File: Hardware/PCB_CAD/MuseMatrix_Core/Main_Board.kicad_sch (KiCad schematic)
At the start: 16 parts, among them J10 Conn_01x03_Pin, J11 Conn_01x03_Pin, J12 Conn_01x03_Pin, J14 Jack-DC, J4 DIN-5, J5 Conn_01x07_Socket, J6 Conn_01x03_Pin, J7 Conn_01x03_Pin, J8 Conn_01x03_Pin, J9 Conn_01x03_Pin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

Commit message: update
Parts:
- J5: value Conn_01x07_Socket -> Conn_01x10_Socket; footprint Connector_JST:JST_EH_B7B-EH-A_1x07_P2.50mm_Vertical -> Library:Skedd connector x10
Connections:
- net jst0: now also J5.1 (Pin_1)
- no-connect marks 4 -> 7
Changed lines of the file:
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@@
 	(paper "A4")
+	(junction
+		(at 38.1 58.38)
+		(diameter 0)
+		(color 0 0 0 0)
+	)
+	(junction
+		(at 38.1 66)
+		(diameter 0)
+		(color 0 0 0 0)
+	)
+	(junction
+		(at 38.1 63.46)
+		(diameter 0)
+		(color 0 0 0 0)
+	)
 	(junction
 		(at 218.6 132.4626)
@@
 	)
 	(junction
+		(at 38.26 68.54)
+		(diameter 0)
+		(color 0 0 0 0)
+	)
+	(junction
 		(at 202 156.3)
+		(diameter 0)
+		(color 0 0 0 0)
+	)
+	(junction
+		(at 38.1 55.88)
+		(diameter 0)
+		(color 0 0 0 0)
+	)
+	(junction
+		(at 37.6 53.34)
 		(diameter 0)
 		(color 0 0 0 0)
@@
 		(color 0 0 0 0)
 	)
+	(junction
+		(at 38.1 60.92)
+		(diameter 0)
+		(color 0 0 0 0)
+	)
+	(no_connect
+		(at 39 71.08)
+	)
 	(no_connect
 		(at 201.08 139.66)
 	)
 	(no_connect
+		(at 39 73.62)
+	)
+	(no_connect
+		(at 39 76.16)
+	)
+	(no_connect
 		(at 208.7 134.58)
 	)
@@
 	(wire
 		(pts
-			(xy 38 63.46) (xy 39 63.46)
+			(xy 36.83 68.58) (xy 36.83 68.54)
+		)
+		(stroke
+			(width 0)
+			(type default)
+		)
+	)
+	(wire
+		(pts
+			(xy 38 63.46) (xy 38.1 63.46)
 		)
 		(stroke
@@
 	(wire
 		(pts
+			(xy 37.6 53.34) (xy 39 53.34)
+		)
+		(stroke
+			(width 0)
+			(type default)
+		)
+	)
+	(wire
+		(pts
+			(xy 38.1 55.88) (xy 39 55.84)
+		)
+		(stroke
+			(width 0)
+			(type default)
+		)
+	)
+	(wire
+		(pts
 			(xy 178.189 131.04) (xy 178.189 131.0479)
 		)
@@
 	(wire
 		(pts
-			(xy 37.8 58.38) (xy 39 58.38)
+			(xy 38.1 66.04) (xy 38.1 66)
+		)
+		(stroke
+			(width 0)
+			(type default)
+		)
+	)
+	(wire
+		(pts
+			(xy 37.8 58.38) (xy 38.1 58.38)
 		)
 		(stroke
@@
 	(wire
 		(pts
-			(xy 38.1 53.4) (xy 39 53.4)
-		)
-		(stroke
-			(width 0)
-			(type default)
-		)
-	)
-	(wire
-		(pts
 			(xy 194.3 128.5) (xy 195.8 128.5)
 		)
@@
 	(wire
 		(pts
-			(xy 37.6 53.26) (xy 37.6 53.3)
+			(xy 37.6 53.26) (xy 37.6 53.34)
+		)
+		(stroke
+			(width 0)
+			(type default)
+		)
+	)
+	(wire
+		(pts
+			(xy 38.26 68.54) (xy 39 68.54)
+		)
+		(stroke
+			(width 0)
+			(type default)
+		)
+	)
+	(wire
+		(pts
+			(xy 38.1 55.84) (xy 38.1 55.88)
 		)
 		(stroke
@@
 	(wire
 		(pts
-			(xy 38.2 68.5) (xy 38.2 68.54)
+			(xy 38.2 68.5) (xy 38.26 68.54)
 		)
 		(stroke
@@
 	(wire
 		(pts
+			(xy 38.1 63.5) (xy 38.1 63.46)
+		)
+		(stroke
+			(width 0)
+			(type default)
+		)
+	)
+	(wire
+		(pts
 			(xy 218.6 138.64) (xy 216.32 138.64)
 		)
@@
 	(wire
 		(pts
-			(xy 37.9 60.92) (xy 39 60.92)
+			(xy 37.9 60.92) (xy 38.1 60.92)
+		)
+		(stroke
+			(width 0)
+			(type default)
+		)
+	)
+	(wire
+		(pts
+			(xy 38.1 66) (xy 39 66)
 		)
 		(stroke
@@
 	(wire
 		(pts
-			(xy 39 53.3) (xy 39 53.4)
+			(xy 39 53.3) (xy 39 53.34)
 		)
 		(stroke
@@
 	(wire
 		(pts
+			(xy 36.83 68.54) (xy 38.26 68.54)
+		)
+		(stroke
+			(width 0)
+			(type default)
+		)
+	)
+	(wire
+		(pts
 			(xy 232.92 160.14) (xy 232.92 157.5217)
 		)
@@
 	(wire
 		(pts
-			(xy 37.6 53.3) (xy 38.26 53.3)
+			(xy 38.1 58.38) (xy 39 58.38)
+		)
+		(stroke
+			(width 0)
+			(type default)
+		)
+	)
+	(wire
+		(pts
+			(xy 36.83 53.34) (xy 37.6 53.34)
+		)
+		(stroke
+			(width 0)
+			(type default)
+		)
+	)
+	(wire
+		(pts
+			(xy 38.1 58.42) (xy 38.1 58.38)
 		)
 		(stroke
@@
 	(wire
 		(pts
-			(xy 38.2 68.54) (xy 39 68.54)
-		)
-		(stroke
-			(width 0)
-			(type default)
-		)
-	)
-	(wire
-		(pts
 			(xy 176.9 136.4) (xy 177.9 136.4)
 		)
@@
 	(wire
 		(pts
-			(xy 38.1 66) (xy 39 66)
-		)
-		(stroke
-			(width 0)
-			(type default)
-		)
-	)
-	(wire
-		(pts
 			(xy 38 63.42) (xy 38 63.46)
 		)
@@
 	(wire
 		(pts
-			(xy 37.7 55.84) (xy 39 55.84)
+			(xy 37.7 55.84) (xy 38.1 55.88)
 		)
 		(stroke
@@
 		)
 	)
+	(wire
+		(pts
+			(xy 38.1 63.46) (xy 39 63.46)
+		)
+		(stroke
+			(width 0)
+			(type default)
+		)
+	)
+	(wire
+		(pts
+			(xy 38.1 60.96) (xy 38.1 60.92)
+		)
+		(stroke
+			(width 0)
+			(type default)
+		)
+	)
+	(wire
+		(pts
+			(xy 38.1 60.92) (xy 39 60.92)
+		)
+		(stroke
+			(width 0)
+			(type default)
+		)
+	)
 	(hierarchical_label "jst3"
 		(shape input)
-		(at 38.26 60.92 180)
+		(at 38.1 60.96 180)
 		(fields_autoplaced yes)
 		(effects
@@
 	(hierarchical_label "jst0"
 		(shape input)
-		(at 38.26 53.3 180)
+		(at 37.49 53.34 180)
 		(fields_autoplaced yes)
 		(effects
@@
 	(hierarchical_label "jst4"
 		(shape input)
-		(at 38.26 63.46 180)
+		(at 38.1 63.5 180)
 		(fields_autoplaced yes)
 		(effects
@@
 	(hierarchical_label "jst5"
 		(shape input)
-		(at 38.26 66 180)
+		(at 38.1 66.04 180)
 		(fields_autoplaced yes)
 		(effects
@@
 	(hierarchical_label "jst1"
 		(shape input)
-		(at 38.26 55.84 180)
+		(at 38.1 55.88 180)
 		(fields_autoplaced yes)
 		(effects
@@
 	(hierarchical_label "jst6"
 		(shape input)
-		(at 38.26 68.54 180)
+		(at 36.83 68.58 180)
 		(fields_autoplaced yes)
 		(effects
@@
 	(hierarchical_label "jst2"
 		(shape input)
-		(at 38.26 58.38 180)
+		(at 38.1 58.42 180)
 		(fields_autoplaced yes)
 		(effects
@@
 			)
 		)
-		(property "Value" "Conn_01x07_Socket"
+		(property "Value" "Conn_01x10_Socket"
 			(at 45.35 65.9999 0)
 			(effects
@@
 			)
 		)
-		(property "Footprint" "Connector_JST:JST_EH_B7B-EH-A_1x07_P2.50mm_Vertical"
+		(property "Footprint" "Library:Skedd connector x10"
 			(at 44.08 63.46 0)
 			(effects

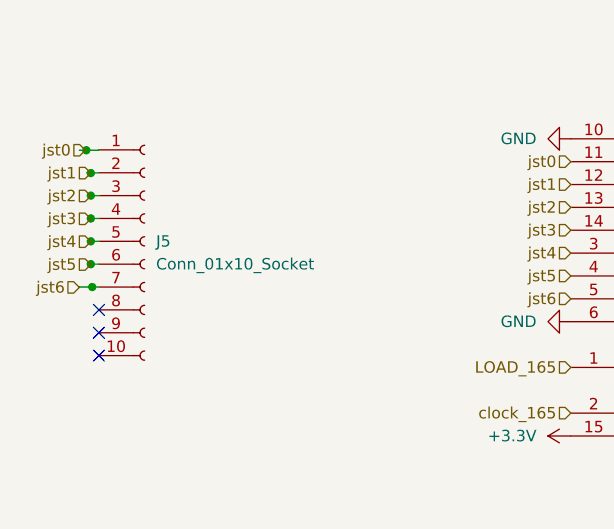
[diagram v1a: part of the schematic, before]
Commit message: separated in 2 boards
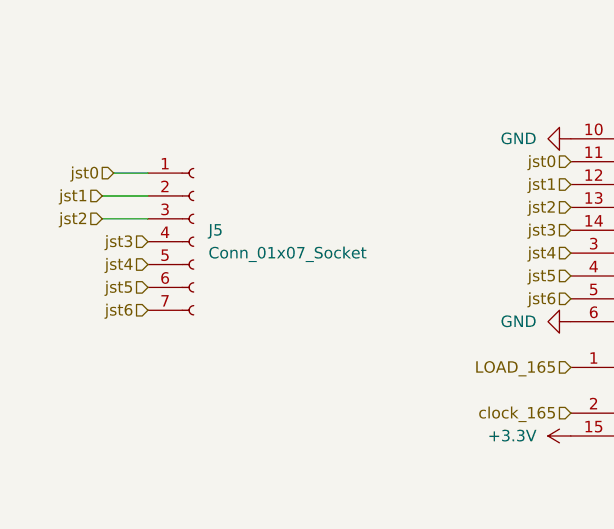
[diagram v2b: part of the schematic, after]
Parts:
- J5: value Conn_01x10_Socket -> Conn_01x07_Socket; footprint Library:Skedd connector x10 -> Connector_PinHeader_1.00mm:PinHeader_1x07_P1.00mm_Horizontal; symbol Connector:Conn_01x10_Socket -> Connector:Conn_01x07_Socket
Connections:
- no-connect marks 7 -> 4
